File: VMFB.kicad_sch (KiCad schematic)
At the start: 136 parts, among them J1 Screw_Terminal_01x02, J10 Conn_01x03_Pin, J11 Conn_01x08_Pin, J12 Conn_01x03_Pin, J13 Conn_01x03_Pin, J14 Conn_01x06_Pin, J15 Conn_01x03_Pin, J16 Conn_01x03_Pin, J17 Conn_01x03_Pin, J18 Conn_01x03_Pin, J19 Conn_01x02_Pin, J2 USB_A_Stacked, J20 Conn_01x03_Pin, J21 Conn_01x02_Pin, J3 USB_B, J4 Barrel_Jack_Switch, J5 Conn_01x02_Pin, J6 Conn_01x03_Pin, J7 Conn_01x02_Pin, J8 Conn_01x03_Pin, J9 Conn_01x03_Pin, Q1 TIP41C, Q2 BC337, Q3 BC547B, Q4 BC547B, Q5 BD139, Q6 BC547B, Q7 BC547B, Q8 BC547, U1 NE555P, U2 NE555P, U3 LM358, U4 NE555P, U5 NE555P

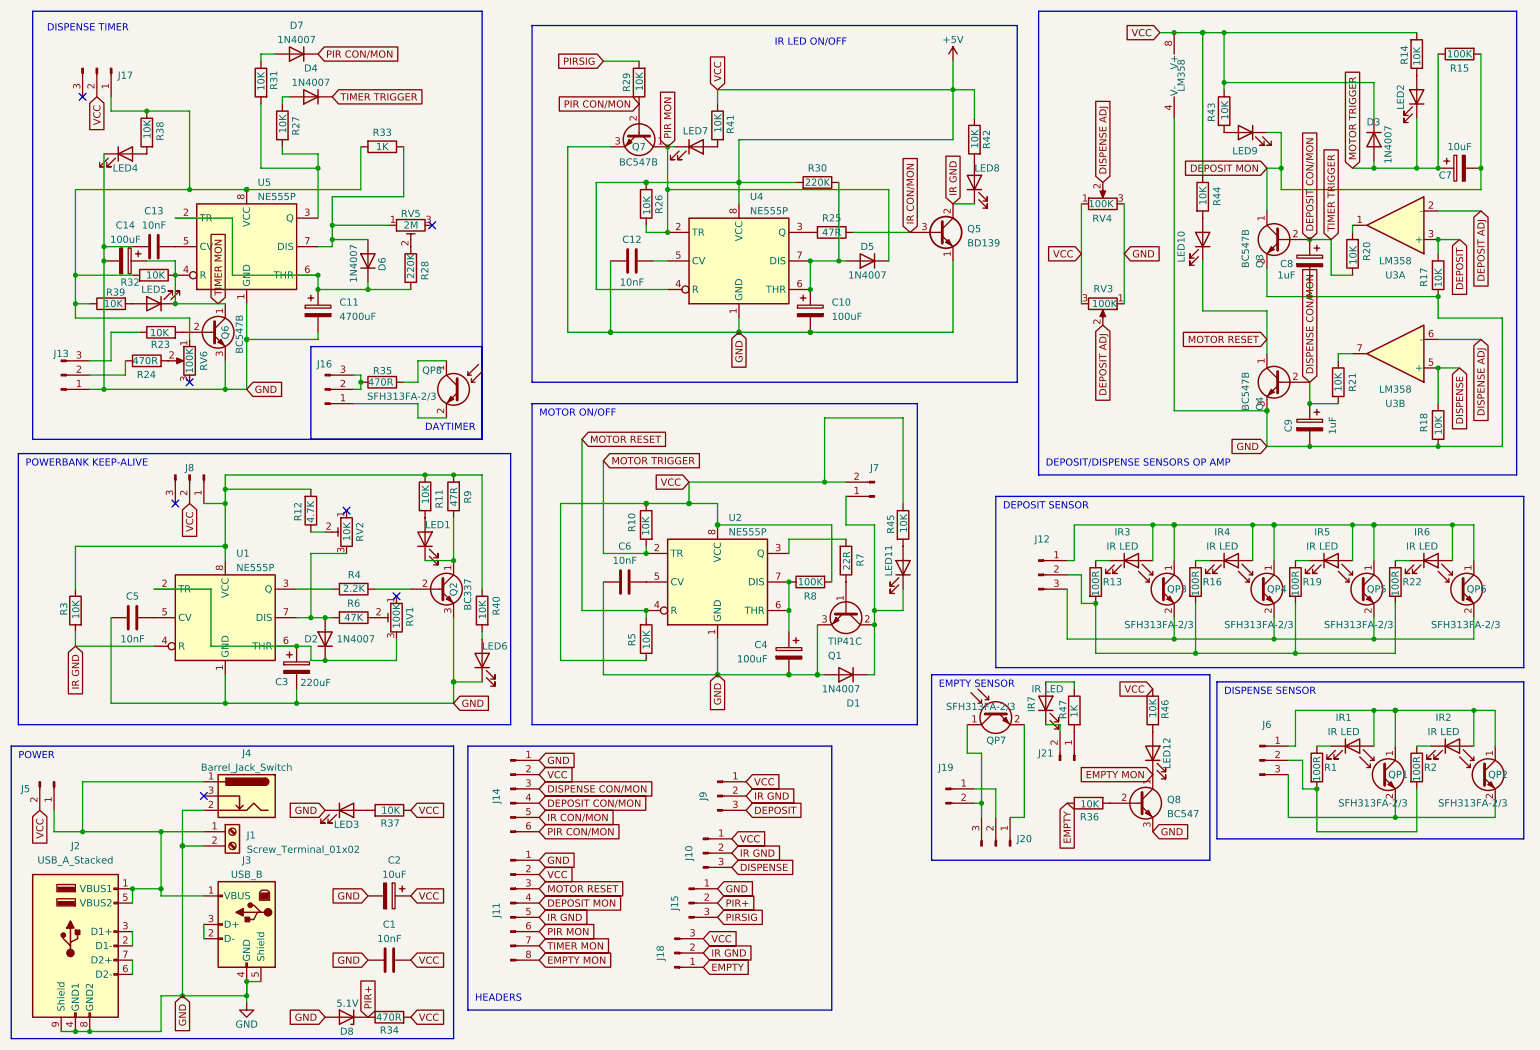
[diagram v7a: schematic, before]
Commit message: fixed dark sensor - connected BC547B emitter to IR GND net (was connected to ground, so base was always triggering the transistor a little due to IR GND being .7 volts above actual ground)
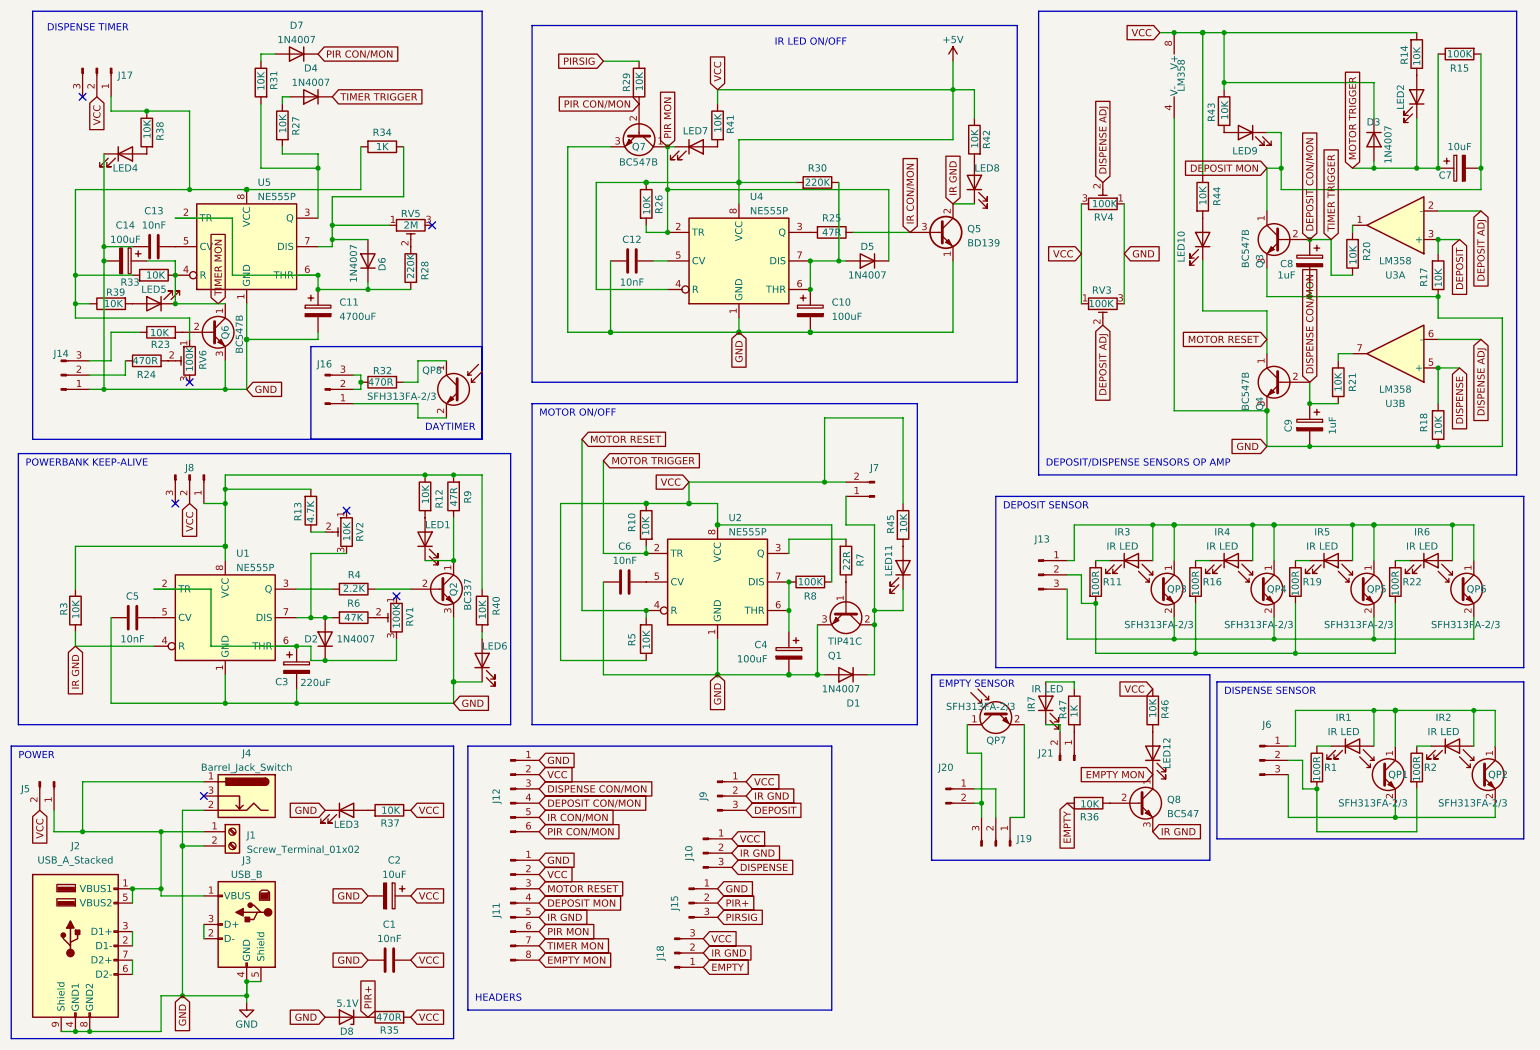
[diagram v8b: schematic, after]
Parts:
- removed RV3, RV4, RV6: 100K, Potentiometer_THT:Potentiometer_Piher_PT-10-V10_Vertical, symbol Device:R_Potentiometer
- added RV3, RV4, RV6: 100K, Potentiometer_THT:Potentiometer_Piher_PT-10-V10_Vertical, symbol Device:R_Potentiometer_Trim
- renumbered J14 to J12, J12 to J13, J13 to J14, J20 to J19, J19 to J20, R13 to R11, R11 to R12, R12 to R13, R35 to R32, R32 to R33, R33 to R34, R34 to R35
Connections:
- net +5V: now also RV3.1, RV4.3
- net DEPOSIT ADJ: now also RV3.2
- net DISPENSE ADJ: now also RV4.2
- net GND: now also RV3.3, RV4.1; no longer Q8.3 (E)
- net IR GND: now also Q8.3 (E)
- net at J17.1 (Pin_1), R33.2, R34.2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: now also RV6.1
- net at R24.2: now also RV6.2
